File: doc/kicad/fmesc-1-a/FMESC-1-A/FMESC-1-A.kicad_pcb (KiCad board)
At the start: 2 copper layers, 48 x 48 mm, 86 parts, among them J1 Conn_01x02, J10 Conn_01x02, J11 Conn_01x02, J12 Conn_01x02, J13 Conn_01x02, J14 Conn_01x02, J15 Conn_01x02, J16 Conn_01x02, J17 Conn_01x02, J18 Conn_01x02, J19 Conn_01x02, J2 Conn_01x02, J20 Conn_01x02, J21 Conn_01x02, J22 Conn_01x02, J23 Conn_01x02, J24 Conn_01x02, J3 Conn_01x02, J4 Conn_01x02, J5 Conn_01x02, J6 Conn_01x02, J7 Conn_01x02, J8 Conn_01x02, J9 Conn_01x02, Q1 AON6504, Q10 AON6504, Q11 AON6504, Q12 AON6504, Q13 AON6504, Q14 AON6504, Q15 AON6504, Q16 AON6504, Q17 AON6504, Q18 AON6504, Q19 AON6504, Q2 AON6504, Q20 AON6504, Q21 AON6504, Q22 AON6504, Q23 AON6504, Q24 AON6504, Q3 AON6504, Q4 AON6504, Q5 AON6504, Q6 AON6504, Q7 AON6504, Q8 AON6504, Q9 AON6504

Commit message: doc/kicad: FMESC-1-A PCB v0.1
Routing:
- net +BATT: track 0.00 -> 231.8 mm
- net GND: track 31.7 -> 251.5 mm, vias 2 -> 40
- net /M4/C1: track 0.00 -> 15.8 mm
- net /M2/A1: track 0.00 -> 15.5 mm
- net /M1/C1: track 0.00 -> 15.4 mm
- net /M4/A1: track 0.00 -> 15.4 mm
- net /M2/C1: track 0.00 -> 15.3 mm
- net /M3/A1: track 0.00 -> 15.3 mm
- net /M4/B1: track 0.00 -> 15.2 mm
- net /M2/B1: track 0.00 -> 15.2 mm
- net /M3/C1: track 0.00 -> 15.2 mm
- net /M3/B1: track 0.00 -> 15.1 mm
- net /M1/A1: track 0.00 -> 15.1 mm
- net /M1/B1: track 0.00 -> 14.9 mm
- net /M2/CLG: track 0.00 -> 2.07 mm
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- added copper zone on B.Cu, net GND
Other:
- board text added: "2020-11-08"
- board text added: "FMESC-1-A v0.1"

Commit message: doc/kicad: FMESC-1-A PCB v0.2
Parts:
- added JT1: Conn_01x02, fmlibf:JS_2P_1.0mm, F.Cu at (68.0, 52.5)
- added JT2: Conn_01x02, fmlibf:JS_2P_1.0mm, F.Cu at (80.0, 53.5)
- added JT3: Conn_01x02, fmlibf:JS_2P_1.0mm, F.Cu at (74.0, 92.5)
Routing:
- net GND: track 251.5 -> 256.5 mm, vias 40 -> 41
- net +BATT: track 231.8 -> 236.8 mm
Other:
- board text added: "2020-11-10"
- board text added: "FMESC-1-A v0.2"
- board text removed: "2020-11-08"
- board text removed: "FMESC-1-A v0.1"

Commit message: doc/kicad: FMESC-1-A v0.3
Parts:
- J1, J10, J11, J12, J13, J14, J15, J16, J17, J18, J19, J2, J20, J21, J22, J23, J24, J3, J4, J5, J6, J7, J8, J9, JT1, JT2, JT3: footprint fmlibf:JS_2P_1.0mm -> fmlibf:JS_2P_1.0mm_F
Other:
- board text added: "2020-11-14"
- board text added: "FMESC-1-A v0.3"
- board text removed: "2020-11-10"
- board text removed: "FMESC-1-A v0.2"

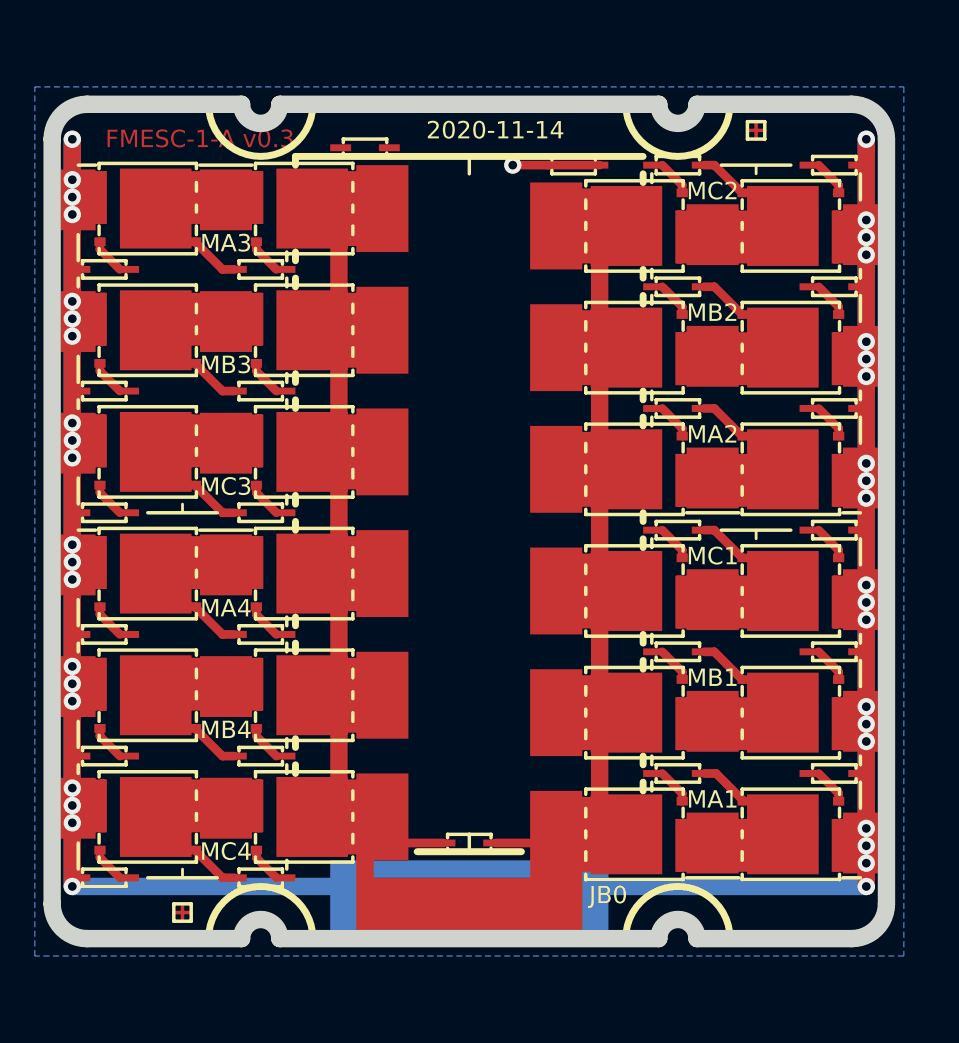
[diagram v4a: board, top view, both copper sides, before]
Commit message: doc/kicad: FMESC-1-A clean and use FMPCBVDL-1
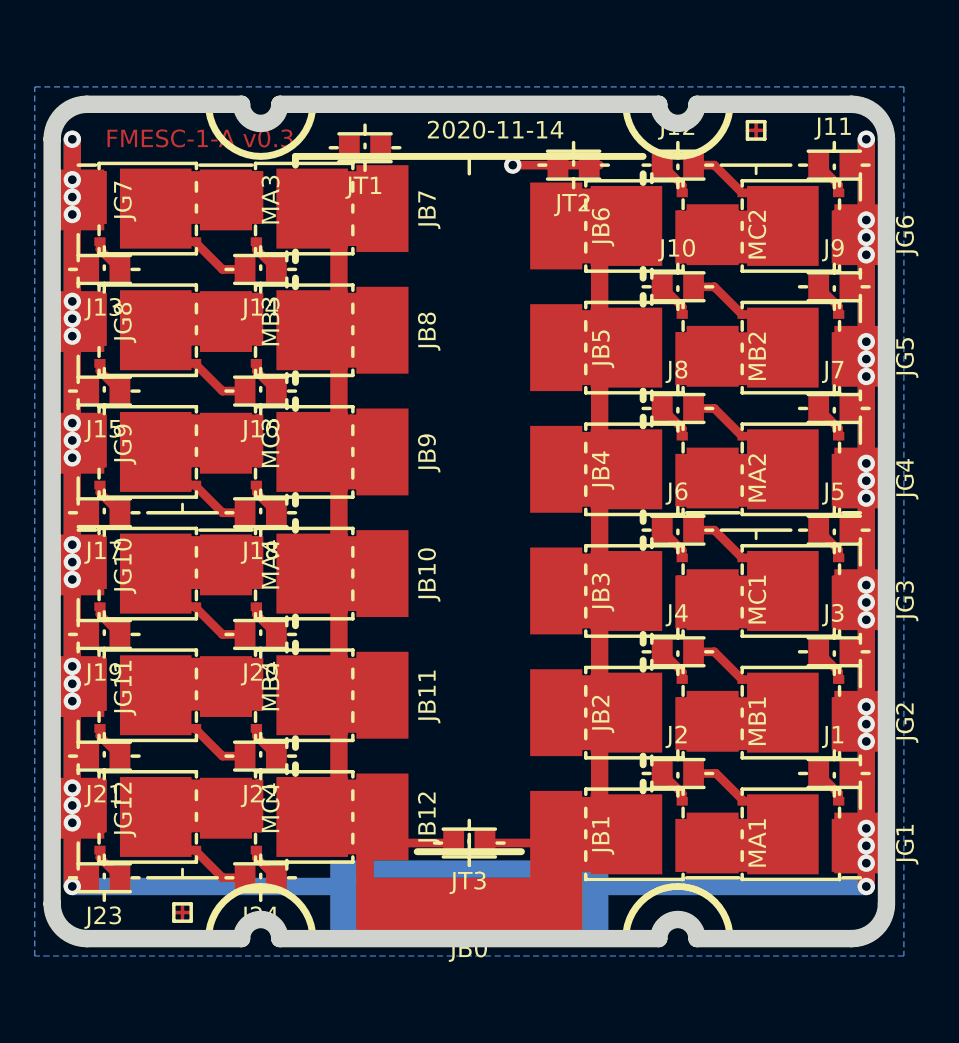
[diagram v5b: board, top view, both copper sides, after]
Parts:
- J1, J10, J11, J12, J13, J14, J15, J16, J17, J18, J19, J2, J20, J21, J22, J23, J24, J3, J4, J5, J6, J7, J8, J9, JT1, JT2, JT3: footprint fmlibf:JS_2P_1.0mm_F -> fmlibf:FMPCBVDL-1-S
- JB0: footprint fmlibf:JS3x13mm -> fmlibf:JS-JB0
- JB1, JB10, JB11, JB12, JB2, JB3, JB4, JB5, JB6, JB7, JB8, JB9: footprint fmlibf:JS3x5mm -> fmlibf:JS-JBx
- JG0: footprint fmlibf:JS4x16mm -> fmlibf:JS-JG0
- JG1, JG10, JG11, JG12, JG2, JG3, JG4, JG5, JG6, JG7, JG8, JG9: footprint fmlibf:JS2x3.5mm -> fmlibf:JS-Jx
- MA1, MA2, MA3, MA4, MB1, MB2, MB3, MB4, MC1, MC2, MC3, MC4: footprint fmlibf:JS3x3.5mm -> fmlibf:JS-Jx

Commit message: doc/kicad: FMESC-1-A v0.3 PCB
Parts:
- JG1, JG10, JG11, JG12, JG2, JG3, JG4, JG5, JG6, JG7, JG8, JG9: footprint fmlibf:JS-Jx -> fmlibf:JS-JGx
- moved JT1 8.08 mm to (65.0, 60.0)
- moved JT2 7.16 mm to (83.0, 60.0)
- moved J1 2.06 mm to (95.5, 90.5), turned to 90 degrees
- moved J10 2.06 mm to (86.5, 62.5), turned to 90 degrees
- moved J11 2.06 mm to (95.5, 55.5), turned to 90 degrees
- moved J12 2.06 mm to (86.5, 55.5), turned to 90 degrees
- moved J13 2.06 mm to (52.5, 57.5), turned to 270 degrees
- moved J14 2.06 mm to (61.5, 57.5), turned to 270 degrees
- moved J15 2.06 mm to (52.5, 64.5), turned to 270 degrees
- moved J16 2.06 mm to (61.5, 64.5), turned to 270 degrees
- moved J17 2.06 mm to (52.5, 71.5), turned to 270 degrees
- moved J18 2.06 mm to (61.5, 71.5), turned to 270 degrees
- moved J19 2.06 mm to (52.5, 78.5), turned to 270 degrees
- moved J2 2.06 mm to (86.5, 90.5), turned to 90 degrees
- moved J20 2.06 mm to (61.5, 78.5), turned to 270 degrees
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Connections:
- JT1 pad 1: Net-(JT1-Pad1) -> GND
- JT1 pad 2: Net-(JT1-Pad2) -> GND
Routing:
- net GND: track 256.5 -> 194.1 mm, vias 41 -> 0
- net +BATT: track 236.8 -> 176.0 mm
- net /M4/C1: track 15.8 -> 9.70 mm
- net /M2/A1: track 15.5 -> 9.50 mm
- net /M4/B1: track 15.2 -> 9.40 mm
- net /M1/C1: track 15.4 -> 9.60 mm
- net /M3/B1: track 15.1 -> 9.30 mm
- net /M2/C1: track 15.3 -> 9.60 mm
- net /M3/A1: track 15.3 -> 9.60 mm
- net /M3/C1: track 15.2 -> 9.50 mm
- net /M4/A1: track 15.4 -> 9.80 mm
- net /M1/B1: track 14.9 -> 9.50 mm
- net /M2/B1: track 15.2 -> 9.80 mm
- net /M1/A1: track 15.1 -> 9.90 mm
- net /M4/CHG: track 2.07 -> 0.90 mm
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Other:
- board size 48 x 48 mm -> 48 x 54 mm
- board text added: "2020-11-29"
- board text removed: "2020-11-14"

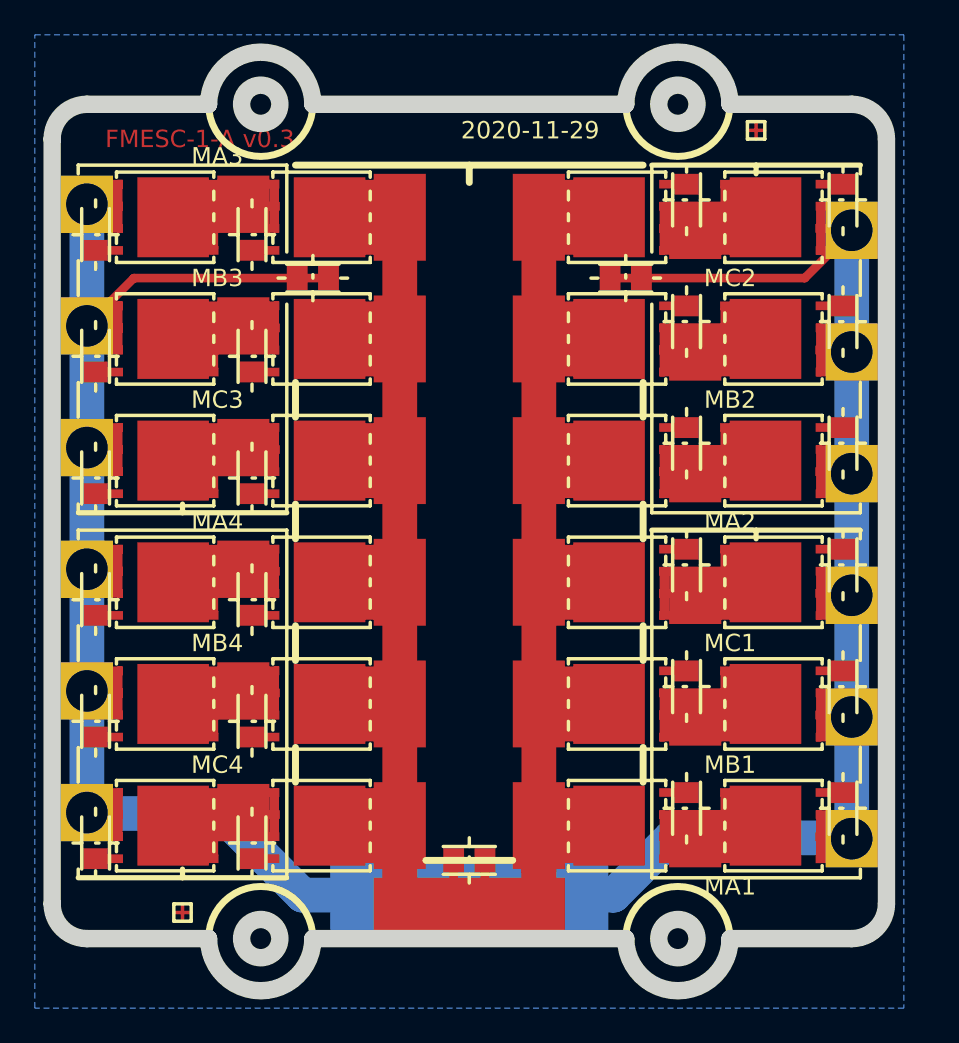
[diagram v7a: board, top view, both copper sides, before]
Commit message: doc/kicad: FMESC-1-A PCB add center hole
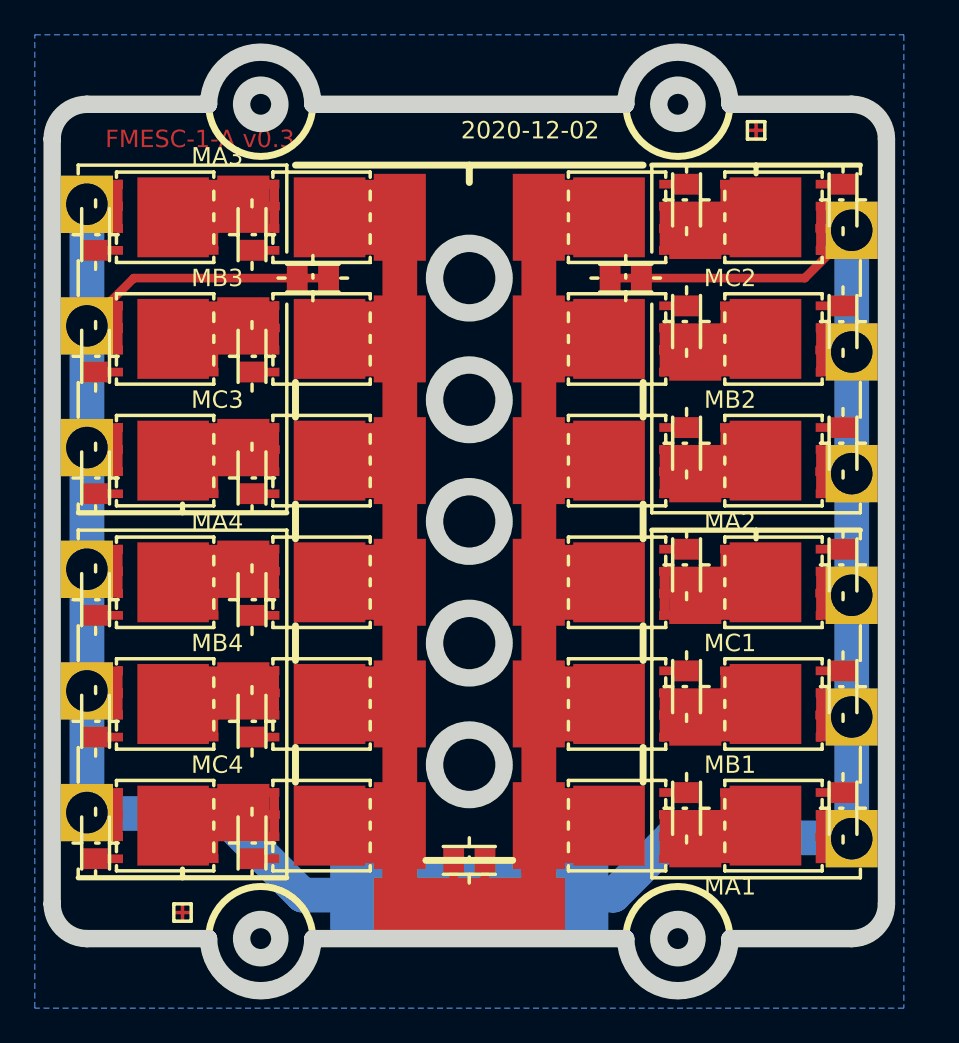
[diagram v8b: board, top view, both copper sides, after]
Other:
- outline, holes or cut-outs redrawn
- board text added: "2020-12-02"
- board text removed: "2020-11-29"
